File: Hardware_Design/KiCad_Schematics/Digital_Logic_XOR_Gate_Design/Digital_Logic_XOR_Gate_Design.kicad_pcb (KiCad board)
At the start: 2 copper layers, 49 x 22.5 mm, 11 parts, among them J1 Conn_01x02_Pin, J2 Conn_01x02_Pin, U1 74LS04, U2 74LS08, U3 74LS32

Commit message: Add PCB design and README for XOR circuit
Designed the internal structure of an XOR gate using basic logic gates to better understand digital systems. Used 2 NOT, 2 AND, and 1 OR gates. Implemented input inverters, AND processing, and final OR combination to achieve the XOR functionality.
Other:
- board text added: "XOR CIRCUIT"
- board text removed: "SELAMLAR"

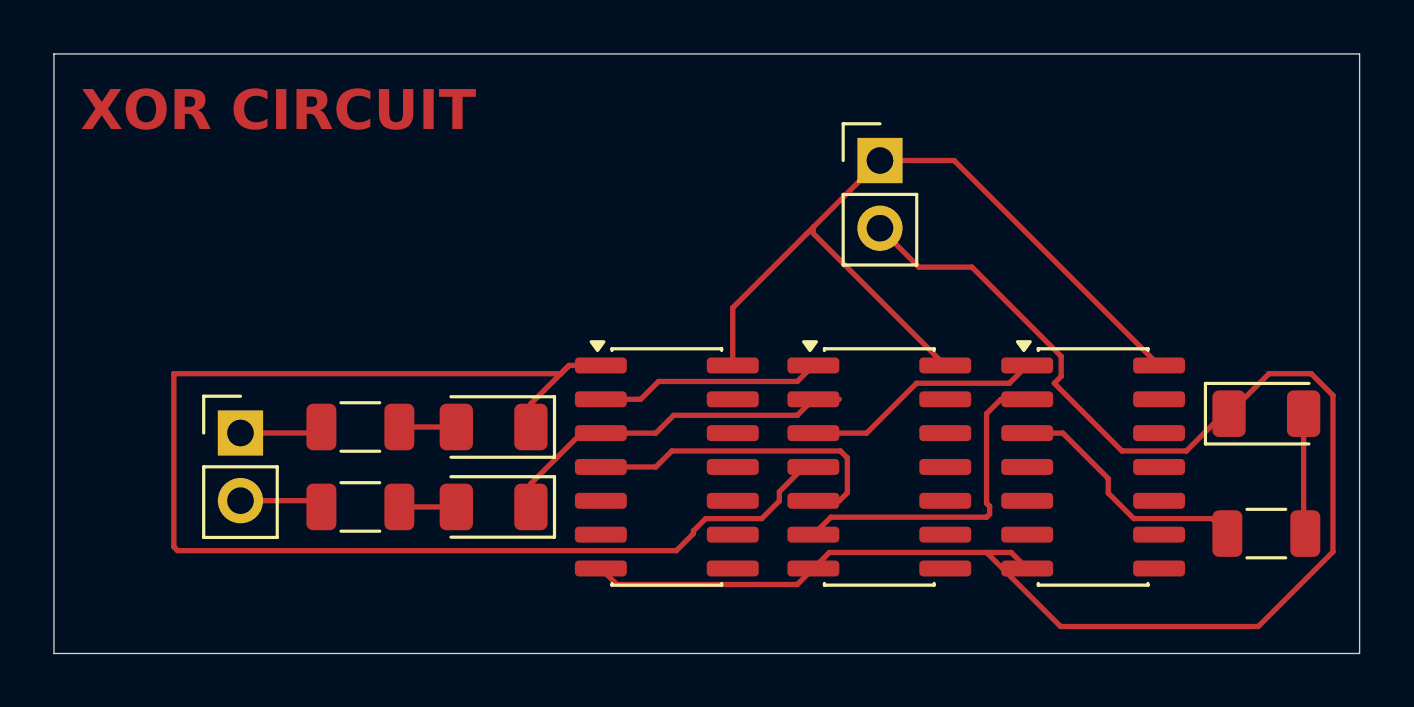
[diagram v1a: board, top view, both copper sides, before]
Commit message: Fix XOR circuit PCB design
Filled the missing ground copper planes.
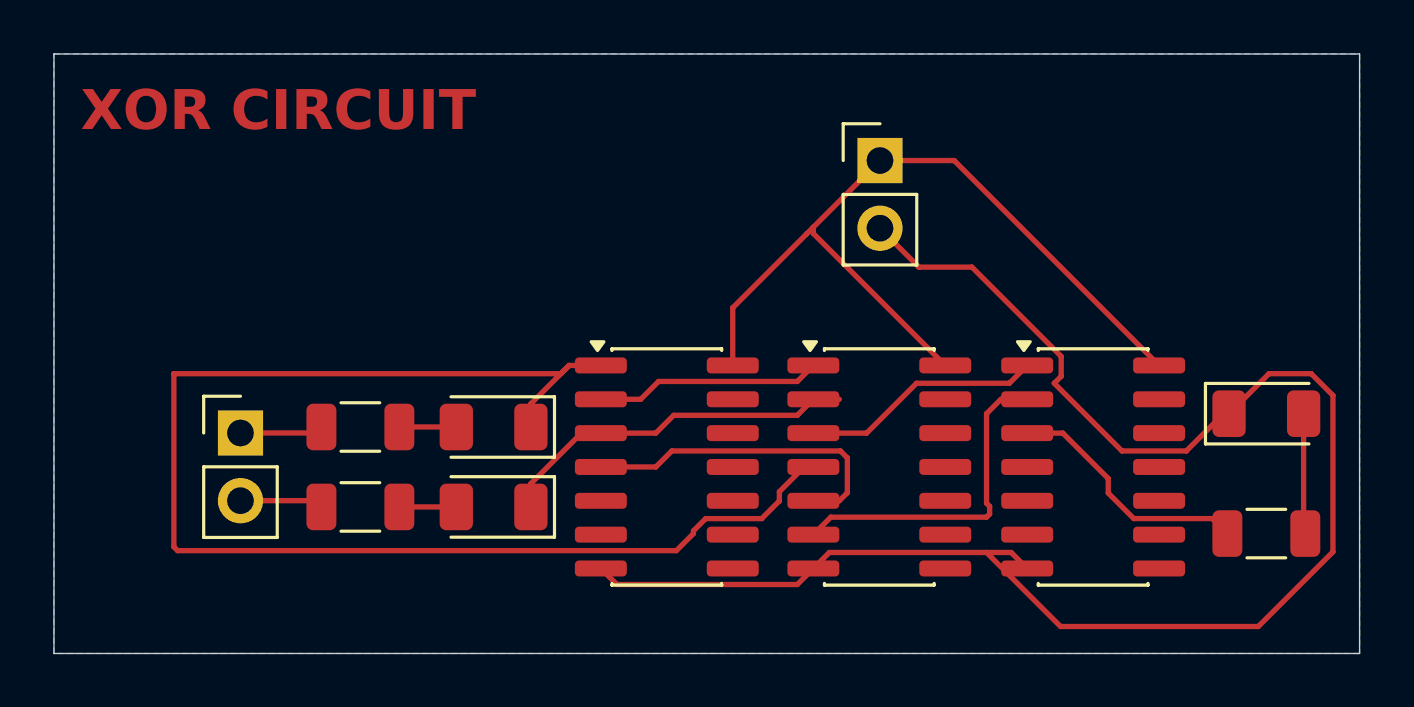
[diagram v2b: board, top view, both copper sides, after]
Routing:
- added copper zone on B.Cu, net GND
